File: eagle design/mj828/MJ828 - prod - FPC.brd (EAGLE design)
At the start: 28 x 22 mm, 5 parts

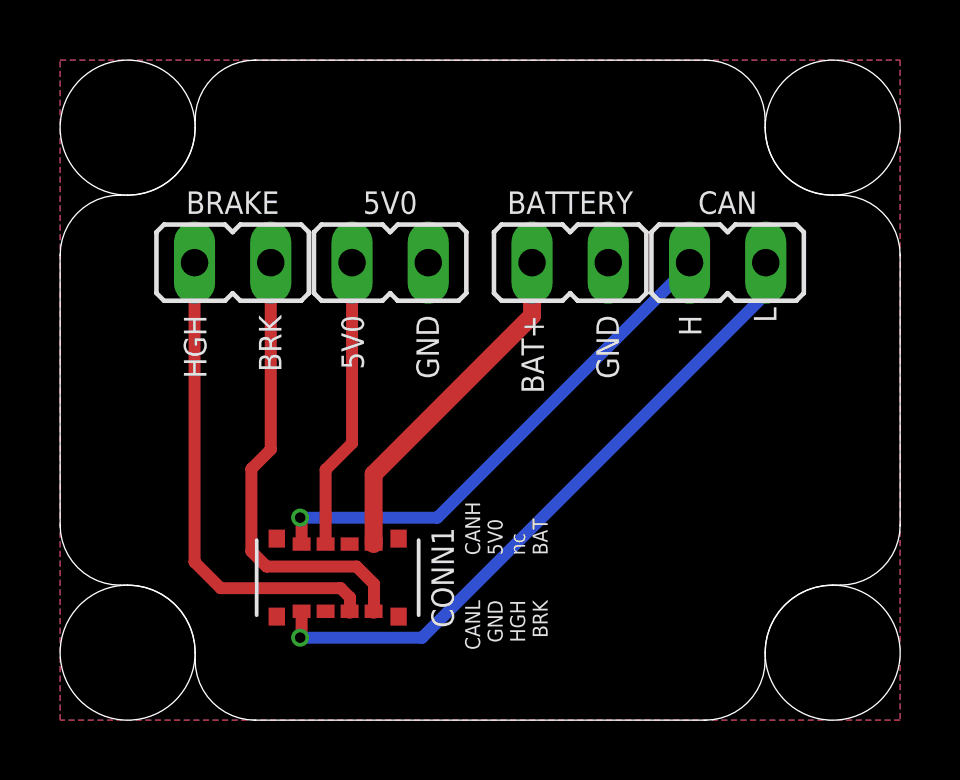
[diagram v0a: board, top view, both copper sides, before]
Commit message: rev.2 board finished. again. - optimized component placement a bit and rerouted
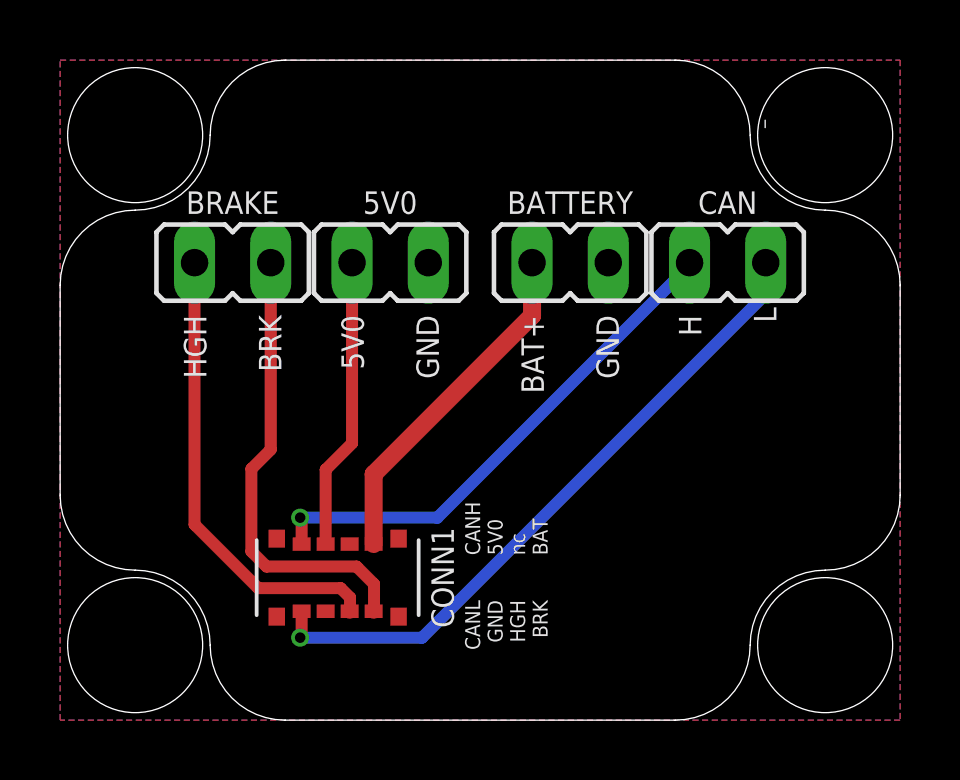
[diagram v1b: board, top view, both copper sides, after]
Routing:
- net HIGH_IN: track 16.1 -> 15.4 mm
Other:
- outline, holes or cut-outs redrawn
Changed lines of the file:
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@@
 <text x="13.75" y="5.5" size="0.5" layer="21" font="vector" rot="R90" align="center-left">CANH</text>
 <text x="13.75" y="4" size="0.5" layer="21" font="vector" rot="R270" align="center-left">CANL</text>
-<wire x1="0" y1="15.5" x2="0" y2="6.5" width="0.01" layer="20"/>
-<wire x1="6.5" y1="0" x2="21.5" y2="0" width="0.01" layer="20"/>
-<wire x1="28" y1="6.5" x2="28" y2="15.5" width="0.01" layer="20"/>
-<wire x1="21.5" y1="22" x2="6.5" y2="22" width="0.01" layer="20"/>
 <wire x1="2" y1="20" x2="14" y2="11" width="0.25" layer="49"/>
 <wire x1="14" y1="11" x2="26" y2="2" width="0.25" layer="49"/>
@@
 <text x="9.75" y="13.5" size="0.75" layer="21" font="vector" rot="R270" align="center-left">5V0</text>
 <text x="15.75" y="13.5" size="0.75" layer="21" font="vector" rot="R270" align="center-left">BAT+</text>
-<wire x1="25.75" y1="4.5" x2="23.5" y2="2.25" width="0.01" layer="20" curve="90"/>
-<wire x1="23.5" y1="19.75" x2="25.75" y2="17.5" width="0.01" layer="20" curve="90"/>
-<wire x1="2.25" y1="17.5" x2="4.5" y2="19.75" width="0.01" layer="20" curve="90"/>
-<wire x1="4.5" y1="2.25" x2="2.25" y2="4.5" width="0.01" layer="20" curve="90"/>
-<wire x1="2.25" y1="4.5" x2="2" y2="4.5" width="0.01" layer="20"/>
-<wire x1="4.5" y1="2.25" x2="4.5" y2="2" width="0.01" layer="20"/>
-<wire x1="23.5" y1="2.25" x2="23.5" y2="2" width="0.01" layer="20"/>
-<wire x1="25.75" y1="4.5" x2="26" y2="4.5" width="0.01" layer="20"/>
-<wire x1="25.75" y1="17.5" x2="26" y2="17.5" width="0.01" layer="20"/>
 <wire x1="23.5" y1="19.75" x2="23.5" y2="20" width="0.01" layer="20"/>
-<wire x1="2.25" y1="17.5" x2="2" y2="17.5" width="0.01" layer="20"/>
-<wire x1="4.5" y1="19.75" x2="4.5" y2="20" width="0.01" layer="20"/>
-<wire x1="23.5" y1="20" x2="21.5" y2="22" width="0.01" layer="20" curve="90"/>
-<wire x1="6.5" y1="22" x2="4.5" y2="20" width="0.01" layer="20" curve="90"/>
-<wire x1="2" y1="17.5" x2="0" y2="15.5" width="0.01" layer="20" curve="90"/>
-<wire x1="0" y1="6.5" x2="2" y2="4.5" width="0.01" layer="20" curve="90"/>
-<wire x1="4.5" y1="2" x2="6.5" y2="0" width="0.01" layer="20" curve="90"/>
-<wire x1="21.5" y1="0" x2="23.5" y2="2" width="0.01" layer="20" curve="90"/>
-<wire x1="26" y1="4.5" x2="28" y2="6.5" width="0.01" layer="20" curve="90"/>
-<hole x="2.25" y="19.75" drill="4.5"/>
-<hole x="25.75" y="19.75" drill="4.5"/>
-<hole x="25.75" y="2.25" drill="4.5"/>
-<hole x="2.25" y="2.25" drill="4.5"/>
-<wire x1="28" y1="15.5" x2="26" y2="17.5" width="0.01" layer="20" curve="90"/>
+<hole x="2.5" y="19.5" drill="4.5"/>
+<hole x="25.5" y="19.5" drill="4.5"/>
+<hole x="25.5" y="2.5" drill="4.5"/>
+<hole x="2.5" y="2.5" drill="4.5"/>
+<wire x1="7.5" y1="0" x2="20.5" y2="0" width="0.01" layer="20"/>
+<wire x1="28" y1="7.5" x2="28" y2="14.5" width="0.01" layer="20"/>
+<wire x1="20.5" y1="22" x2="7.5" y2="22" width="0.01" layer="20"/>
+<wire x1="0" y1="14.5" x2="0" y2="7.5" width="0.01" layer="20"/>
+<wire x1="2.5" y1="5" x2="5" y2="2.5" width="0.01" layer="20" curve="-90"/>
+<wire x1="23" y1="2.5" x2="25.5" y2="5" width="0.01" layer="20" curve="-90"/>
+<wire x1="25.5" y1="17" x2="23" y2="19.5" width="0.01" layer="20" curve="-90"/>
+<wire x1="5" y1="19.5" x2="2.5" y2="17" width="0.01" layer="20" curve="-90"/>
+<wire x1="25.5" y1="17" x2="28" y2="14.5" width="0.01" layer="20" curve="-90"/>
+<wire x1="20.5" y1="22" x2="23" y2="19.5" width="0.01" layer="20" curve="-90"/>
+<wire x1="5" y1="19.5" x2="7.5" y2="22" width="0.01" layer="20" curve="-90"/>
+<wire x1="0" y1="14.5" x2="2.5" y2="17" width="0.01" layer="20" curve="-90"/>
+<wire x1="2.5" y1="5" x2="0" y2="7.5" width="0.01" layer="20" curve="-90"/>
+<wire x1="7.5" y1="0" x2="5" y2="2.5" width="0.01" layer="20" curve="-90"/>
+<wire x1="23" y1="2.5" x2="20.5" y2="0" width="0.01" layer="20" curve="-90"/>
+<wire x1="28" y1="7.5" x2="25.5" y2="5" width="0.01" layer="20" curve="-90"/>
 </plain>
 <attributes>
@@
 <contactref element="CONN1" pad="P$6"/>
 <contactref element="BRAKE" pad="1"/>
-<wire x1="4.48" y1="15.25" x2="4.48" y2="5.27" width="0.4" layer="1"/>
-<wire x1="4.48" y1="5.27" x2="5.35" y2="4.4" width="0.4" layer="1"/>
+<wire x1="4.48" y1="15.25" x2="4.48" y2="6.52" width="0.4" layer="1"/>
+<wire x1="4.48" y1="6.52" x2="6.6" y2="4.4" width="0.4" layer="1"/>
 <wire x1="9.6624" y1="4.0876" x2="9.6624" y2="3.6424" width="0.4" layer="1"/>
 <wire x1="9.65" y1="3.63" x2="9.6624" y2="3.6424" width="0.5" layer="1"/>
 <wire x1="9.35" y1="4.4" x2="9.6624" y2="4.0876" width="0.4" layer="1"/>
-<wire x1="5.35" y1="4.4" x2="9.35" y2="4.4" width="0.4" layer="1"/>
+<wire x1="6.6" y1="4.4" x2="9.35" y2="4.4" width="0.4" layer="1"/>
 </signal>
 </signals>

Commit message: - changed 0804 LEDs to 1206, rerouted, added relevant datasheets - added BOM (includes FPC board to board connector) - created MJ828 autocad housing drawing
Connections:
- net CANH: now also CAN.1, CONN1.P$8; no longer CAN.2, CONN1.P$1
- net CANL: now also CAN.2, CONN1.P$1; no longer CAN.1, CONN1.P$8
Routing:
- net CANL: track 22.2 -> 17.5 mm
- net CANH: track 17.5 -> 22.2 mm
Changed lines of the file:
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@@
 <text x="19.5" y="8.75" size="1" layer="29" font="vector" align="center">MJ-828 FPC
 ejovrh v.1</text>
-<text x="13.75" y="5.5" size="0.5" layer="21" font="vector" rot="R90" align="center-left">CANH</text>
-<text x="13.75" y="4" size="0.5" layer="21" font="vector" rot="R270" align="center-left">CANL</text>
+<text x="13.75" y="5.5" size="0.5" layer="21" font="vector" rot="R90" align="center-left">CANL</text>
+<text x="13.75" y="4" size="0.5" layer="21" font="vector" rot="R270" align="center-left">CANH</text>
 <wire x1="2" y1="20" x2="14" y2="11" width="0.25" layer="49"/>
 <wire x1="14" y1="11" x2="26" y2="2" width="0.25" layer="49"/>
@@
 <text x="12.25" y="13.5" size="0.75" layer="21" font="vector" rot="R270" align="center-left">GND</text>
 <text x="18.25" y="13.5" size="0.75" layer="21" font="vector" rot="R270" align="center-left">GND</text>
-<text x="21" y="13.5" size="0.75" layer="21" font="vector" rot="R270" align="center-left">H</text>
-<text x="23.5" y="13.25" size="0.75" layer="21" font="vector" rot="R90" align="center-left">L</text>
+<text x="23.5" y="13.25" size="0.75" layer="21" font="vector" rot="R270" align="center">H</text>
+<text x="21" y="13.25" size="0.75" layer="21" font="vector" rot="R90" align="center">L</text>
 <text x="7" y="13.5" size="0.75" layer="21" font="vector" rot="R270" align="center-left">BRK</text>
 <text x="4.5" y="13.5" size="0.75" layer="21" font="vector" rot="R270" align="center-left">HGH</text>
@@
 </signal>
 <signal name="CANH" class="3">
-<contactref element="CONN1" pad="P$1"/>
-<contactref element="CAN" pad="2"/>
-<via x="8" y="6.75" extent="1-16" drill="0.35"/>
-<wire x1="8" y1="6.75" x2="8.05" y2="6.7" width="0.4" layer="1"/>
-<wire x1="8.05" y1="6.7" x2="8.05" y2="5.87" width="0.4" layer="1"/>
-<wire x1="8" y1="6.75" x2="12.57354375" y2="6.75" width="0.4" layer="16"/>
-<wire x1="20.98" y1="15.15645625" x2="20.98" y2="15.25" width="0.4" layer="16"/>
-<wire x1="12.57354375" y1="6.75" x2="20.98" y2="15.15645625" width="0.4" layer="16"/>
-</signal>
-<signal name="CANL" class="3">
 <contactref element="CONN1" pad="P$8"/>
 <contactref element="CAN" pad="1"/>
 <via x="8" y="2.75" extent="1-16" drill="0.35"/>
-<wire x1="8.05" y1="3.63" x2="8.05" y2="2.8" width="0.4" layer="1"/>
-<wire x1="8.05" y1="2.8" x2="8" y2="2.75" width="0.4" layer="1"/>
 <wire x1="12.06149375" y1="2.748" x2="8" y2="2.748" width="0.4" layer="16"/>
 <wire x1="8" y1="2.75" x2="8" y2="2.748" width="0.5" layer="16"/>
 <wire x1="23.52" y1="15.25" x2="23.52" y2="14.20650625" width="0.4" layer="16"/>
 <wire x1="23.52" y1="14.20650625" x2="12.06149375" y2="2.748" width="0.4" layer="16"/>
+<wire x1="8.05" y1="3.63" x2="8.05" y2="2.8" width="0.4" layer="1"/>
+<wire x1="8.05" y1="2.8" x2="8" y2="2.75" width="0.4" layer="1"/>
+</signal>
+<signal name="CANL" class="3">
+<contactref element="CONN1" pad="P$1"/>
+<contactref element="CAN" pad="2"/>
+<via x="8" y="6.75" extent="1-16" drill="0.35"/>
+<wire x1="8" y1="6.75" x2="12.57354375" y2="6.75" width="0.4" layer="16"/>
+<wire x1="20.98" y1="15.15645625" x2="20.98" y2="15.25" width="0.4" layer="16"/>
+<wire x1="12.57354375" y1="6.75" x2="20.98" y2="15.15645625" width="0.4" layer="16"/>
+<wire x1="8.05" y1="5.87" x2="8.05" y2="6.7" width="0.4" layer="1"/>
+<wire x1="8.05" y1="6.7" x2="8" y2="6.75" width="0.4" layer="1"/>
 </signal>
 <signal name="5V0" class="2">
